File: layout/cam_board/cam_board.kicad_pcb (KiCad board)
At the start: 4 copper layers, 60 x 45 mm, 78 parts, among them J2 USB Connector, J3 BATT_CONNECTOR, J4 LCD conn, J5 Stick conn, J6 Conn_01x05_Pin, M1 MountingHole_2.1mm, M2 MountingHole_2.1mm, SW1 BOOT0, SW2 NRST, SW3 USER, SW4 ON/OFF, U1 STM32F401CCUx, U2 USBLC6-2SC6, U3 M24C16-RMN6TP, U4 AP2112K-3.3, U5 MCP73871-1AA, Y1 ECS-80-18-23B-JTN-TR, Y2 SC32S-7PF20PPM

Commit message: Update board and layout
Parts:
- removed J6: Conn_01x05_Pin, Connector_PinHeader_1.27mm:PinHeader_1x05_P1.27mm_Vertical
- added J1: Conn_01x06_Pin, Connector_PinHeader_1.27mm:PinHeader_1x06_P1.27mm_Vertical, F.Cu at (126.0, 60.8)
- added JP5: SolderJumper_2_Open, Jumper:SolderJumper-2_P1.3mm_Open_RoundedPad1.0x1.5mm, F.Cu at (122.4, 61.0)
- added JP6: SolderJumper_2_Open, Jumper:SolderJumper-2_P1.3mm_Open_RoundedPad1.0x1.5mm, F.Cu at (112.7, 58.0)
- moved R19 4.38 mm to (111.1, 61.0), turned to 180 degrees
- moved D4 2.75 mm to (107.6, 61.0), turned to 0 degrees
- moved D5 1.67 mm to (119.0, 63.2), turned to -90 degrees
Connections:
- C17 pad 1: +3V3 -> Net-(JP6-A)
- U4 pad 5: +3V3 -> Net-(JP6-A)
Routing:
- net Net-(JP6-A): track 0.00 -> 4.24 mm
- net Net-(J1-Pin_1): track 0.00 -> 3.05 mm
- net +3V3: track 61.6 -> 63.9 mm, vias 20 -> 23
- net VIN: track 55.3 -> 53.3 mm
- net SWDIO: track 33.0 -> 34.9 mm
- net Net-(D5-A): track 13.0 -> 11.1 mm
- net GND: track 98.7 -> 97.8 mm, vias 125 -> 124
- net NRST: track 73.3 -> 74.0 mm

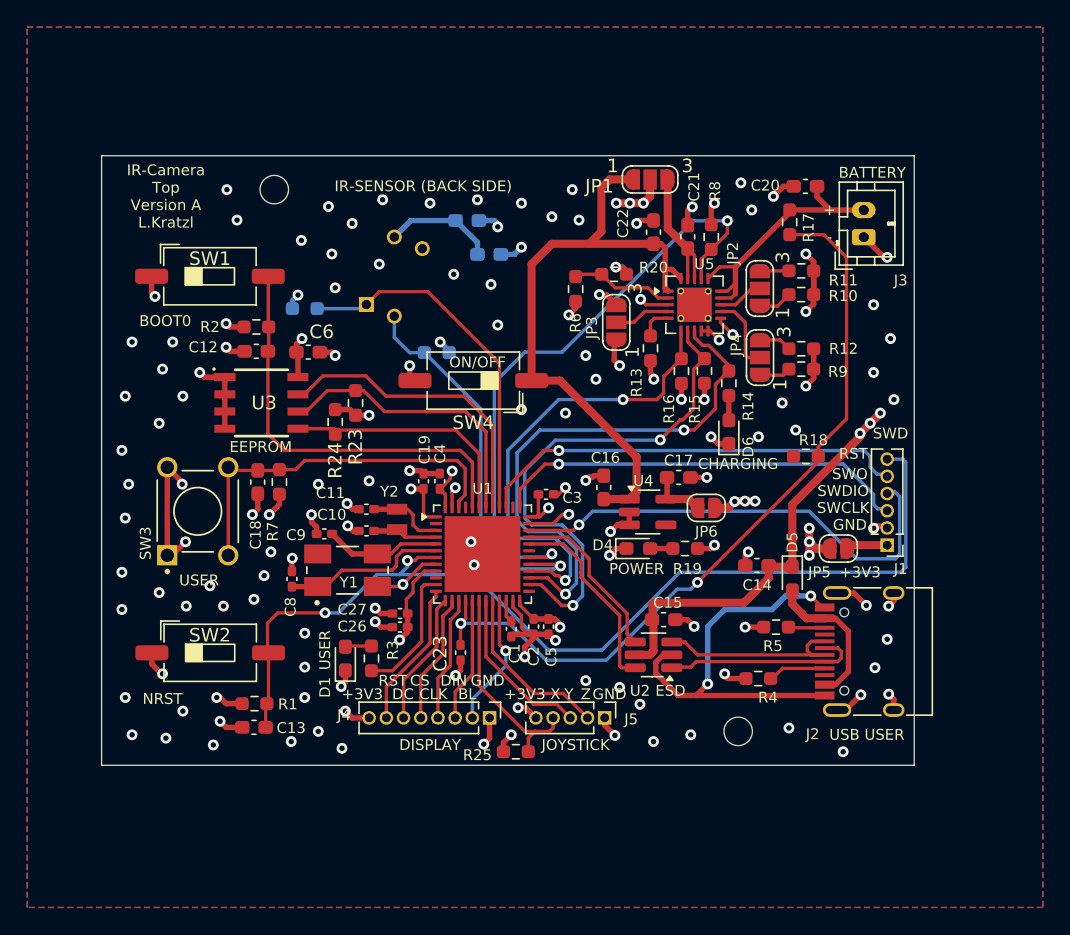
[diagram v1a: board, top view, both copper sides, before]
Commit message: add to main loop, update layout and schematic
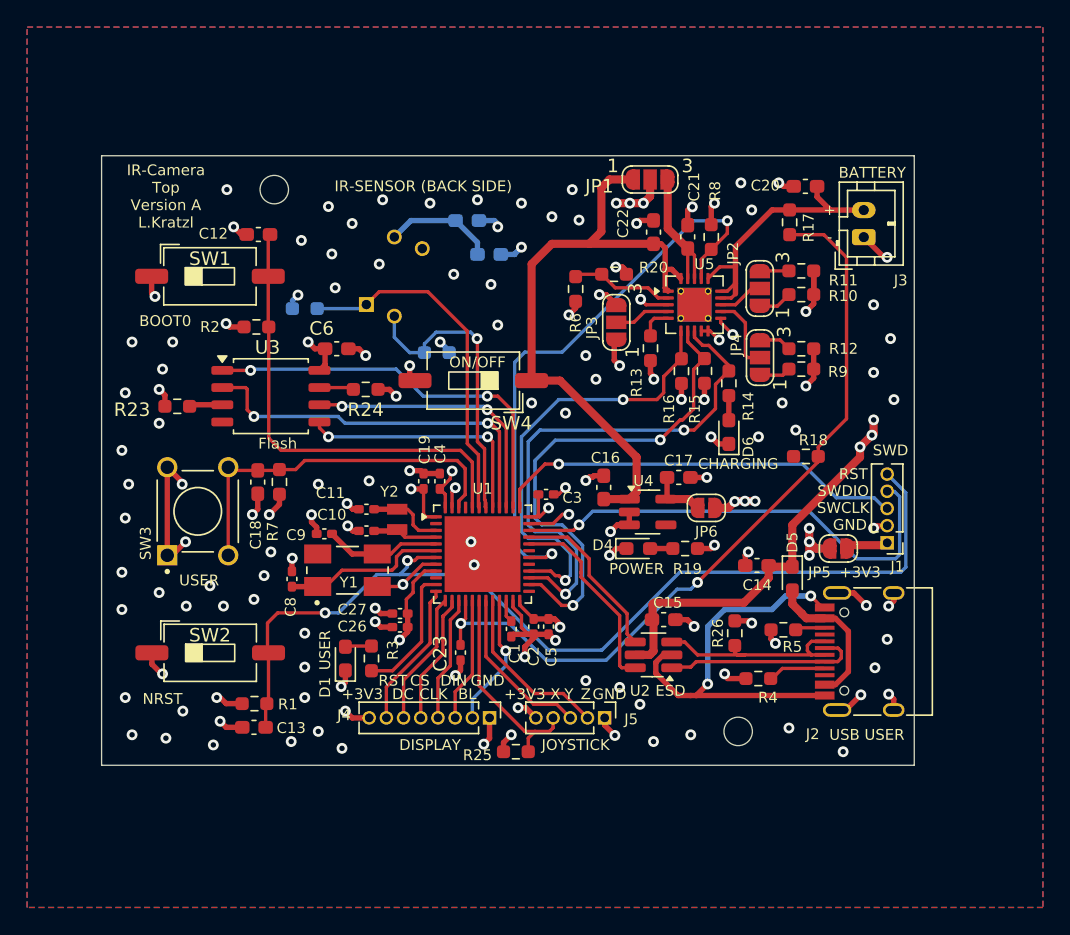
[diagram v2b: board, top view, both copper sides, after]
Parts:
- added R26: 1k5, Resistor_SMD:R_0603_1608Metric_Pad0.98x0.95mm_HandSolder, F.Cu at (114.8, 67.2)
- J1: value Conn_01x06_Pin -> Conn_01x05_Pin; footprint Connector_PinHeader_1.27mm:PinHeader_1x06_P1.27mm_Vertical -> Connector_PinHeader_1.27mm:PinHeader_1x05_P1.27mm_Vertical
- U3: value M24C16-RMN6TP -> W25Q128JVS; footprint A_Custom:SOIC127P600X175-8N -> Package_SO:SOIC-8_5.3x5.3mm_P1.27mm
- moved R23 13.2 mm to (73.6, 50.5), turned to 180 degrees
- moved C12 8.63 mm to (79.6, 37.8)
- moved R24 3.29 mm to (87.5, 49.2), turned to 0 degrees
- moved C6 2.13 mm to (85.4, 46.2)
- moved U3 0.86 mm to (80.5, 49.8)
- moved R5 0.57 mm to (118.3, 67.0)
- moved J1 0.17 mm to (126.0, 60.6)
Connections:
- J1 pad 5: SWO -> NRST
- R23 pad 1: EEPROM_SCL -> Net-(U3-~{WP}/IO_{2})
- R24 pad 1: +3V3 -> Net-(U3-~{HOLD}/~{RESET}/IO_{3})
- R24 pad 2: EEPROM_SDA -> +3V3
- U1 pad 29: SCL -> unconnected-(U1-PA8-Pad29)
- U1 pad 38: unconnected-(U1-PA15-Pad38) -> FLASH_CS
- U1 pad 39: SWO -> FLASH_SCK
- U1 pad 40: SDA -> FLASH_MISO
- U1 pad 41: EEPROM_NWC -> FLASH_MOSI
- U1 pad 42: EEPROM_SCL -> SCL
- U1 pad 43: EEPROM_SDA -> SDA
- U3 pad 1: GND -> FLASH_CS
- U3 pad 2: GND -> FLASH_MISO
- U3 pad 3: GND -> Net-(U3-~{WP}/IO_{2})
- U3 pad 5: EEPROM_SDA -> FLASH_MOSI
- U3 pad 6: EEPROM_SCL -> FLASH_SCK
- U3 pad 7: EEPROM_NWC -> Net-(U3-~{HOLD}/~{RESET}/IO_{3})
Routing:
- net SWO: track 32.0 -> 0.00 mm, vias 1 -> 0
- net FLASH_CS: track 0.00 -> 29.9 mm, vias 0 -> 2
- net FLASH_MISO: track 0.00 -> 28.3 mm, vias 0 -> 2
- net EEPROM_NWC: track 22.5 -> 0.00 mm
- net EEPROM_SCL: track 21.4 -> 0.00 mm
- net FLASH_SCK: track 0.00 -> 20.4 mm, vias 0 -> 2
- net FLASH_MOSI: track 0.00 -> 18.5 mm, vias 0 -> 2
- net EEPROM_SDA: track 18.1 -> 0.00 mm
- net SCL: track 29.4 -> 22.1 mm
- net GND: track 97.8 -> 91.1 mm, vias 124 -> 121
- net BOOT0: track 31.0 -> 34.3 mm
- net Net-(U3-~{HOLD}/~{RESET}/IO_{3}): track 0.00 -> 2.56 mm
- net Net-(U3-~{WP}/IO_{2}): track 0.00 -> 2.46 mm
- net VIN: track 53.3 -> 51.2 mm, vias 15 -> 14
- net NRST: track 74.0 -> 72.2 mm
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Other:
- board text added: "Flash"
- board text removed: "EEPROM"
- board text removed: "SWO"

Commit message: Update layout
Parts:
- moved C26 3.76 mm to (90.0, 63.0), turned to -90 degrees
- moved C10 3.38 mm to (86.8, 56.4)
- moved C11 3.38 mm to (86.8, 54.8)
- moved Y2 3.38 mm to (89.0, 55.6)
- moved C9 3.35 mm to (86.8, 57.5)
- moved R3 3.01 mm to (87.8, 66.1), turned to 180 degrees
- moved C27 2.93 mm to (91.0, 63.0), turned to -90 degrees
- moved Y1 2.45 mm to (85.4, 60.3)
- moved D1 2.24 mm to (87.7, 67.7), turned to 180 degrees
- moved C8 2.12 mm to (80.7, 61.6), turned to 0 degrees
- moved R18 1.95 mm to (120.0, 52.2)
- moved C3 1.65 mm to (101.5, 58.5)
- moved C2 1.47 mm to (101.4, 66.9), turned to 180 degrees
- moved C16 1.19 mm to (104.2, 57.3), turned to 180 degrees
- moved JP5 1.04 mm to (123.0, 60.1), turned to -90 degrees
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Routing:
- net GND: track 91.1 -> 69.3 mm, vias 121 -> 64
- net +3V3: track 65.6 -> 49.3 mm, vias 25 -> 20
- net VIN: track 51.2 -> 44.5 mm, vias 14 -> 16
- net USER_LED: track 9.74 -> 5.00 mm
- net OSC32_IN: track 5.65 -> 9.19 mm
- net EXT_POWER: track 33.4 -> 29.8 mm
- net BATTLVL: track 57.9 -> 61.3 mm
- net OSC32_OUT: track 4.84 -> 8.12 mm
- net BATTCHARGING: track 39.8 -> 36.5 mm
- net BATTFULL: track 37.1 -> 35.1 mm
- net STICK_X: track 15.7 -> 17.5 mm
- net OSC_IN: track 8.59 -> 7.42 mm
- net NRST: track 72.2 -> 73.3 mm
- net VOUT: track 46.3 -> 47.3 mm
- net Net-(J2-D+-PadA6): track 15.2 -> 14.5 mm
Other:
- board text added: "+3V3 ext"

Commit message: Update layout
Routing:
- net BOOT0: track 34.2 -> 32.9 mm
- net GND: track 69.3 -> 70.4 mm, vias 64 -> 66
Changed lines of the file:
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@@
 	)
 	(segment
+		(start 93.875 56.1)
+		(end 93.2375 55.4625)
+		(width 0.4)
+		(layer "F.Cu")
+		(net 1)
+	)
+	(segment
 		(start 81.13125 57)
 		(end 81.13125 57.86875)
@@
 	)
 	(segment
+		(start 93.875 56.1)
+		(end 93.875 57.9725)
+		(width 0.25)
+		(layer "F.Cu")
+		(net 1)
+	)
+	(segment
 		(start 107.9 42.7)
 		(end 108.2 43)
@@
 	)
 	(segment
+		(start 125.31 59.31)
+		(end 124.9 58.9)
+		(width 0.25)
+		(layer "F.Cu")
+		(net 1)
+	)
+	(segment
 		(start 88.6 67.7)
 		(end 89.7 67.7)
@@
 	)
 	(segment
+		(start 126 59.31)
+		(end 125.31 59.31)
+		(width 0.25)
+		(layer "F.Cu")
+		(net 1)
+	)
+	(segment
 		(start 98.25 60.7)
 		(end 97.8 60.7)
@@
 	)
 	(segment
+		(start 93.2375 55.4625)
+		(end 92.9725 55.4625)
+		(width 0.4)
+		(layer "F.Cu")
+		(net 1)
+	)
+	(segment
 		(start 98.2 63.5)
 		(end 98.2 63.2)
@@
 	)
 	(segment
-		(start 93.875 57.9725)
-		(end 93.875 55.775)
-		(width 0.25)
-		(layer "F.Cu")
-		(net 1)
-	)
-	(segment
 		(start 94 63.5)
 		(end 94 63.25)
@@
 	)
 	(segment
-		(start 93.875 55.775)
-		(end 93.5625 55.4625)
-		(width 0.25)
-		(layer "F.Cu")
-		(net 1)
-	)
-	(segment
 		(start 107.9 42.475)
 		(end 107.9 42.7)
@@
 	)
 	(segment
-		(start 93.5625 55.4625)
-		(end 92.9725 55.4625)
-		(width 0.25)
-		(layer "F.Cu")
-		(net 1)
-	)
-	(segment
 		(start 94 60.75)
 		(end 94.5 60.75)
@@
 	)
 	(via
+		(at 93.875 56.1)
+		(size 0.8)
+		(drill 0.4)
+		(layers "F.Cu" "B.Cu")
+		(net 1)
+	)
+	(via
 		(at 111.275 36.025)
 		(size 0.8)
@@
 	)
 	(via
-		(at 83.7 56.7)
-		(size 0.8)
-		(drill 0.4)
-		(layers "F.Cu" "B.Cu")
-		(net 1)
-	)
-	(via
 		(at 102.987347 58.487347)
 		(size 0.8)
@@
 	)
 	(via
+		(at 124.9 58.9)
+		(size 0.8)
+		(drill 0.4)
+		(layers "F.Cu" "B.Cu")
+		(net 1)
+	)
+	(via
 		(at 102.8 65.8)
 		(size 0.8)
@@
 	)
 	(via
+		(at 89.4 57.8)
+		(size 0.8)
+		(drill 0.4)
+		(layers "F.Cu" "B.Cu")
+		(net 1)
+	)
+	(via
 		(at 79.53125 57.96875)
 		(size 0.8)
@@
 	(segment
 		(start 120 55)
-		(end 122.25 57.25)
+		(end 121.8 56.8)
 		(width 0.25)
 		(layer "B.Cu")
@@
 	)
 	(segment
-		(start 122.25 57.25)
-		(end 125.04 57.25)
+		(start 121.8 56.8)
+		(end 124.59 56.8)
 		(width 0.25)
 		(layer "B.Cu")
@@
 	)
 	(segment
-		(start 125.04 57.25)
+		(start 124.59 56.8)
 		(end 126 58.21)
 		(width 0.25)
@@
 	)
 	(segment
-		(start 95.375 57.9725)
-		(end 95.375 54.625)
+		(start 80.305 44.60125)
+		(end 80.3425 44.63875)
 		(width 0.25)
 		(layer "F.Cu")
@@
 	)
 	(segment
-		(start 80.305 44.60125)
-		(end 80.3425 44.63875)
+		(start 93.95 53.2)
+		(end 83 53.2)
 		(width 0.25)
 		(layer "F.Cu")
@@
 	)
 	(segment
-		(start 93.95 53.2)
-		(end 80.7 53.2)
+		(start 80.305 40.89875)
+		(end 80.305 44.60125)
 		(width 0.25)
 		(layer "F.Cu")
@@
 	)
 	(segment
-		(start 95.375 54.625)
-		(end 93.95 53.2)
+		(start 81.2 51.4)
+		(end 81.2 45.49625)
 		(width 0.25)
 		(layer "F.Cu")
@@
 	)
 	(segment
-		(start 80.305 40.89875)
-		(end 80.305 44.60125)
+		(start 81.2 45.49625)
+		(end 80.3425 44.63875)
 		(width 0.25)
 		(layer "F.Cu")
@@
 	)
 	(segment
-		(start 80.3425 52.8425)
-		(end 80.3425 44.63875)
+		(start 95.375 57.9725)
+		(end 95.375 54.625)
 		(width 0.25)
 		(layer "F.Cu")
@@
 	)
 	(segment
-		(start 80.7 53.2)
-		(end 80.3425 52.8425)
+		(start 83 53.2)
+		(end 81.2 51.4)
 		(width 0.25)
 		(layer "F.Cu")
@@
 	)
 	(segment
+		(start 95.375 54.625)
+		(end 93.95 53.2)
+		(width 0.25)
+		(layer "F.Cu")
+		(net 16)
+	)
+	(segment
 		(start 80.305 37.945)
 		(end 80.4375 37.8125)
@@
 	(segment
 		(start 123 59.5)
-		(end 121.5 59.5)
+		(end 123 58)
 		(width 0.6)
 		(layer "F.Cu")
@@
 	)
 	(segment
+		(start 123 58)
+		(end 122.9 57.9)
+		(width 0.6)
+		(layer "F.Cu")
+		(net 52)
+	)
+	(segment
 		(start 98.875 64.8475)
 		(end 99.38 64.8475)
@@
 	)
 	(segment
-		(start 120.75 59.5)
-		(end 119.9 59.5)
-		(width 0.6)
-		(layer "F.Cu")
-		(net 52)
-	)
-	(segment
 		(start 93.375 57.9725)
 		(end 93.375 57)
@@
 	)
 	(segment
+		(start 122.05 57.9)
+		(end 122.9 57.9)
+		(width 0.6)
+		(layer "F.Cu")
+		(net 52)
+	)
+	(segment
 		(start 90 63.605)
 		(end 89.135 63.605)
@@
 	)
 	(segment
-		(start 121.5 59.5)
-		(end 120.75 59.5)
+		(start 122.9 57.9)
+		(end 123.65 57.9)
 		(width 0.6)
 		(layer "F.Cu")
@@
 	)
 	(via
-		(at 121.5 59.5)
+		(at 123.65 57.9)
 		(size 0.8)
 		(drill 0.4)
@@
 	)
 	(via
-		(at 120.75 59.5)
+		(at 122.9 57.9)
 		(size 0.8)
 		(drill 0.4)
@@
 	)
 	(via
-		(at 119.9 59.5)
+		(at 122.05 57.9)
 		(size 0.8)
 		(drill 0.4)
@@
 	)
 	(segment
+		(start 124 53.5)
+		(end 124 54)
+		(width 0.6)
+		(layer "F.Cu")
+		(net 58)
+	)
+	(segment
 		(start 108.675 66)
 		(end 108.75 66.075)
@@
 	)
 	(segment
-		(start 124 54)
-		(end 119 59)
-		(width 0.6)
-		(layer "F.Cu")
-		(net 58)
-	)
-	(segment
 		(start 124 52)
 		(end 124 52.75)
@@
 	)
 	(segment
-		(start 124 53.5)
-		(end 124 54)
-		(width 0.6)
-		(layer "F.Cu")
-		(net 58)
-	)
-	(segment
 		(start 112.5125 49.9875)
 		(end 112.5 50)
@@
 	)
 	(segment
+		(start 120.3 61)
+		(end 119 62.3)
+		(width 0.6)
+		(layer "F.Cu")
+		(net 58)
+	)
+	(segment
 		(start 114.3 54.275)
 		(end 114.3 53.2875)
@@
 	)
 	(segment
+		(start 120.3 57.7)
+		(end 120.3 61)
+		(width 0.6)
+		(layer "F.Cu")
+		(net 58)
+	)
+	(segment
 		(start 108.675 66)
 		(end 108.8 66)
@@
 	)
 	(segment
-		(start 119 59)
+		(start 119 62.3)
 		(end 119 62.34)
 		(width 0.6)
@@
 		(layer "F.Cu")
 		(net 58)
+	)
+	(segment
+		(start 124 54)
+		(end 120.3 57.7)
+		(width 0.6)
+		(layer "F.Cu")
+		(net 58)

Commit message: Update layout
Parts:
- added R27: 100k, Resistor_SMD:R_0603_1608Metric_Pad0.98x0.95mm_HandSolder, F.Cu at (103.9, 53.1)
- C24, C25, R21, R22: moved to F.Cu
- moved C24 5.31 mm to (92.0, 36.8)
- moved SW4 4.31 mm to (99.8, 48.8), turned to -90 degrees
- moved C25 3.54 mm to (91.9, 35.0)
- moved R22 2.75 mm to (92.5, 43.8)
- moved R21 1.93 mm to (84.9, 43.0)
- moved C16 1.32 mm to (105.0, 56.2), turned to 90 degrees
- moved M1 0.75 mm to (80.0, 34.5)
- moved R24 0.61 mm to (86.9, 49.1)
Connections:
- SW4 pad 2: GND -> Net-(U4-EN)
- U4 pad 3: GND -> Net-(U4-EN)
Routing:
- net Net-(U4-EN): track 0.00 -> 12.2 mm
- net SDA: track 26.2 -> 20.8 mm
- net +3V3: track 49.4 -> 45.1 mm
- net BATTLVL: track 61.3 -> 58.3 mm
- net VOUT: track 47.3 -> 44.3 mm
- net SCL: track 22.1 -> 19.2 mm, vias 1 -> 0
- net Net-(U2-GND): track 30.4 -> 32.5 mm
- net BL: track 9.86 -> 11.9 mm
- net SWDIO: track 35.1 -> 33.7 mm
- net BATTFULL: track 35.1 -> 34.1 mm
- net Net-(J3-Pin_2): track 20.8 -> 21.6 mm
- net BATTCHARGING: track 36.5 -> 35.9 mm
- net SWCLK: track 30.5 -> 31.1 mm
- net BOOT0: track 32.9 -> 33.5 mm
- net FLASH_CS: track 29.9 -> 30.5 mm
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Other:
- board text added: "IR-SENSOR"

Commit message: Update
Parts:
- removed the SW2 at (76.0, 68.7)
- added SW3: NRST, A_Custom:SW_1825910-6-4, F.Cu at (75.1, 67.4)
- moved C8 0.40 mm to (79.1, 74.5)
- moved R7 0.40 mm to (79.1, 72.8)
- renumbered C10 to C1, C26 to C10, C27 to C11, C6 to C12, C1 to C13, C19 to C14, C2 to C15, C3 to C16, C4 to C17, C5 to C18, C16 to C19, C12 to C2, C17 to C20, C15 to C23, C23 to C24, C20 to C25, C14 to C26, C18 to C3, C8 to C4, C11 to C5, C9 to C6, C24 to C7, C13 to C8, C25 to C9, D4 to D2, D5 to D3, D6 to D4, J5 to J1, J4 to J2, J1 to J3, J2 to J4, J3 to J5, JP3 to JP1, JP4 to JP3, JP5 to JP4, JP6 to JP5, JP1 to JP6, R22 to R1, R9 to R12, R8 to R13, R12 to R14, R6 to R15, R20 to R16, R27 to R17, R13 to R18, R21 to R2, R16 to R20, R4 to R21, R5 to R22, R17 to R23, R14 to R24, R26 to R25, R15 to R26, R18 to R27, R2 to R3, R7 to R4, R25 to R5, R3 to R6, R1 to R7, R23 to R8, R24 to R9, SW3 to SW2, U3 to U1, U1 to U2, U4 to U3, U5 to U4, U2 to U5, Y2 to Y1, Y1 to Y2
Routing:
- net NRST: track 73.3 -> 83.2 mm
- net GND: track 70.5 -> 75.3 mm, vias 211 -> 194
